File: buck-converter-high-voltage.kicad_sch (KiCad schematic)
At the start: 18 parts, among them J1 Input, U1 MAX17574

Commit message: Finished PCB
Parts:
- added C10: 100nF 63V, Capacitor_SMD:C_0603_1608Metric, symbol Device:C
- added J2: Output, Connector_PinHeader_2.54mm:PinHeader_2x02_P2.54mm_Horizontal, symbol Connector_Generic:Conn_02x02_Counter_Clockwise
- added R5: 100k, Resistor_SMD:R_0603_1608Metric, symbol Device:R
- C1, C2, C3, C4, C5, C8, C9: footprint (none) -> Capacitor_SMD:C_0603_1608Metric
- C6, C7: value 22uF -> 22uF 10V; footprint (none) -> Capacitor_SMD:C_0805_2012Metric
- JP1, JP2: footprint (none) -> extraFootprints:SolderJumper-Open_0603
- L1: footprint (none) -> Inductor_SMD:L_Coilcraft_XAL6060-XXX
- R1, R2, R3, R4: footprint (none) -> Resistor_SMD:R_0603_1608Metric
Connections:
- net +6V: now also J2.1 (Pin_1), J2.2 (Pin_2)
- net EN: now also R5.2
- net GND: now also C10.2, J2.3 (Pin_3), J2.4 (Pin_4), R5.1
- net Vdrive: now also C10.1
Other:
- moved on the sheet: JP1, JP2, R3

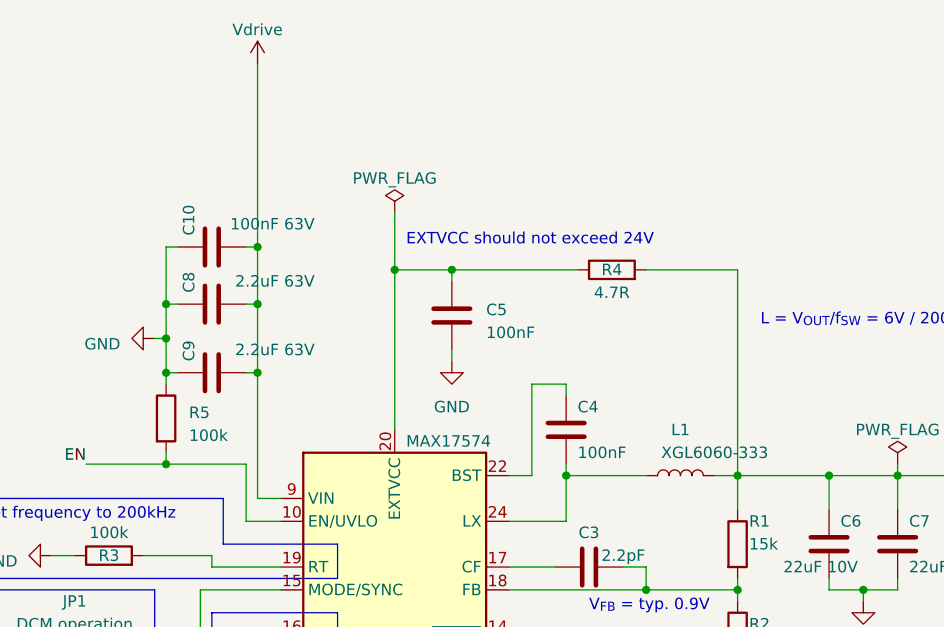
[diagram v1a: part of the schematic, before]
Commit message: Change inductor value to 47µH
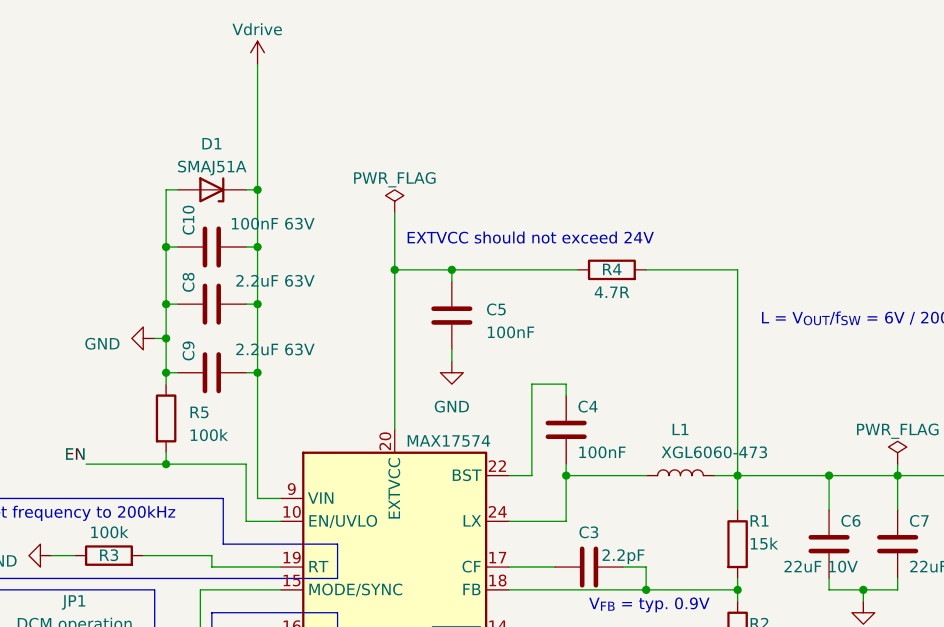
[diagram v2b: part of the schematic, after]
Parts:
- added D1: SMAJ51A, Diode_SMD:D_SMA, symbol Device:D_Zener
- L1: value XGL6060-333 -> XGL6060-473
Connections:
- net GND: now also D1.2 (A)
- net Vdrive: now also D1.1 (K)
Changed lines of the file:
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@@
   (junction (at 143.51 54.61) (diameter 0) (color 0 0 0 0)
   )
+  (junction (at 143.51 41.91) (diameter 0) (color 0 0 0 0)
+  )
   (junction (at 78.74 49.53) (diameter 0) (color 0 0 0 0)
   )
@@
   )
   (junction (at 196.85 86.36) (diameter 0) (color 0 0 0 0)
+  )
+  (junction (at 133.35 48.26) (diameter 0) (color 0 0 0 0)
   )
   (junction (at 133.35 58.42) (diameter 0) (color 0 0 0 0)
@@
     (stroke (width 0) (type default))
   )
-  (wire (pts (xy 143.51 48.26) (xy 143.51 27.94))
+  (wire (pts (xy 143.51 48.26) (xy 143.51 41.91))
     (stroke (width 0) (type default))
   )
@@
     (stroke (width 0) (type default))
   )
+  (wire (pts (xy 133.35 48.26) (xy 133.35 41.91))
+    (stroke (width 0) (type default))
+  )
   (wire (pts (xy 214.63 85.09) (xy 214.63 86.36))
     (stroke (width 0) (type default))
@@
     (stroke (width 0) (type default))
   )
+  (wire (pts (xy 143.51 27.94) (xy 143.51 41.91))
+    (stroke (width 0) (type default))
+  )
   (polyline (pts (xy 133.35 111.76) (xy 133.35 115.57))
     (stroke (width 0) (type default))
@@
     (stroke (width 0) (type default))
   )
+  (wire (pts (xy 142.24 41.91) (xy 143.51 41.91))
+    (stroke (width 0) (type default))
+  )
   (wire (pts (xy 196.85 50.8) (xy 196.85 73.66))
     (stroke (width 0) (type default))
@@
   )
   (polyline (pts (xy 152.4 85.09) (xy 137.16 85.09))
+    (stroke (width 0) (type default))
+  )
+  (wire (pts (xy 133.35 41.91) (xy 134.62 41.91))
     (stroke (width 0) (type default))
   )
@@
     )
   )
+  (symbol (lib_id "Device:D_Zener") (at 138.43 41.91 180) (unit 1)
+    (in_bom yes) (on_board yes) (dnp no) (fields_autoplaced)
+    (property "Reference" "D1" (at 138.43 36.83 0)
+      (effects (font (size 1.27 1.27)))
+    )
+    (property "Value" "SMAJ51A" (at 138.43 39.37 0)
+      (effects (font (size 1.27 1.27)))
+    )
+    (property "Footprint" "Diode_SMD:D_SMA" (at 138.43 41.91 0)
+      (effects (font (size 1.27 1.27)) hide)
+    )
+    (property "Datasheet" "~" (at 138.43 41.91 0)
+      (effects (font (size 1.27 1.27)) hide)
+    )
+    (pin "1")
+    (pin "2")
+    (instances
+      (project "buck-converter-high-voltage"
+        (path "/8a19eb0d-d01a-4f25-a0f7-e48b79171dc2"
+          (reference "D1") (unit 1)
+        )
+      )
+    )
+  )
   (symbol (lib_id "Connector_Generic:Conn_02x02_Counter_Clockwise") (at 72.39 80.01 0) (unit 1)
     (in_bom yes) (on_board yes) (dnp no)
@@
       (effects (font (size 1.27 1.27)))
     )
-    (property "Value" "XGL6060-333" (at 194.31 71.12 90)
-      (effects (font (size 1.27 1.27)))
-    )
+    (property "Value" "XGL6060-473" (at 194.31 71.12 90)
+      (effects (font (size 1.27 1.27)))
+    )
